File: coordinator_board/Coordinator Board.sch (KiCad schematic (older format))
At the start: 19 parts, among them P1 POWER, P4 SERIAL, SW1 Switch_SPDT_x2, SW2 Switch_DPST, U1 LM3671, U3 ESP-12E, U4 DIY-OLED-0.96, U5 SF303GJ26

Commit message: Finished updated schematic
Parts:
- removed P1: POWER, PH_Connector:S2B-PH-K-S, symbol CONN_01X02
- removed R8: 0, Resistors_SMD:R_0805_HandSoldering, symbol R
- added J1, J2, J3, J4: Conn_01x04, Pin_Headers:Pin_Header_Angled_1x04_Pitch2.54mm, symbol Conn_01x04
- added U6, U7: CD40109B, Housings_SSOP:TSSOP-24_4.4x7.8mm_Pitch0.65mm, symbol CD40109B
- added U8: 10118194, symbol 10118194
- R7: value 0 -> R
- RP1: footprint R_Array:R_Array_Concave_4x0805 -> nebrius-discrete:R_Array_Concave_4x0805
- SW2: footprint KMR6:KMR641NG -> nebrius-switch:KMR641NG
- U4: footprint DIY-OLED:DIY-OLED-0.96 -> nebrius-lcd:DIY-OLED-0.96
- U5: footprint SF303GJ26:SF303GJ26 -> nebrius-switch:SF303GJ26
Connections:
- net labels added: +5V
- wire segments 84 -> 177
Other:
- moved on the sheet: C1, C2, L1, P4, R1, R2, R4, R5, R6, RP1, SW1A, SW2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

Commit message: Fixed ESP footprint
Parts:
- U3: footprint ESP8266:ESP-12 -> ESP8266:ESP-12E_SMD
- U8: footprint (none) -> nebrius-conn:10118194
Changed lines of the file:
@@
 F 0 "U3" H 7400 4450 50  0000 C CNN
 F 1 "ESP-12E" H 7400 4650 50  0000 C CNN
-F 2 "ESP8266:ESP-12" H 7400 4550 50  0001 C CNN
+F 2 "ESP8266:ESP-12E_SMD" H 7400 4550 50  0001 C CNN
 F 3 "" H 7400 4550 50  0001 C CNN
 	1    7400 4550
@@
 F 0 "U8" V 1350 4950 60  0000 C CNN
 F 1 "10118194" H 1750 5050 60  0000 C CNN
-F 2 "" H 1850 4750 60  0001 C CNN
+F 2 "nebrius-conn:10118194" H 1850 4750 60  0001 C CNN
 F 3 "" H 1850 4750 60  0001 C CNN
 	1    1850 4750

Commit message: Finalized first draft of new schematic
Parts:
- removed U8: 10118194, nebrius-conn:10118194, symbol 10118194
- added D1: LED, LEDs:LED_1206_HandSoldering, symbol LED
- added R8: 0, Resistors_SMD:R_0805_HandSoldering, symbol R
- added U0: 10118194, nebrius-conn:10118194, symbol 10118194
- R7: value R -> 10k
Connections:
- net +5V: now also C1.1, SW1.2 (B), U1.1 (VIN), U1.3 (EN); no longer SW1.1 (A)
- net GND: now also R8.2, U0.5 (GND)
- net at U3.20 (GPIO10): now also D1.2 (A)
- new net: SW1.1 (A), U0.1 (Vcc)
- new net: D1.1 (K), R8.1
- no-connect marks 9 -> 8
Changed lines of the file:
@@
 EESchema Schematic File Version 2
+LIBS:Coordinator Board-rescue
 LIBS:power
 LIBS:device
@@
 	3600 4600 3650 4600
 Wire Wire Line
-	3750 4050 3750 4250
-Wire Wire Line
-	3750 4250 2600 4250
+	3750 4250 3750 3700
+Wire Wire Line
+	2600 4250 3750 4250
 Wire Wire Line
 	2600 4250 2600 4350
@@
 	8550 6400 10150 6400
 Wire Wire Line
-	10150 6400 10150 3500
+	10150 6400 10150 3550
 $Comp
 L Conn_01x04 J1
@@
 	1    0    0    -1
 $EndComp
-Connection ~ 2450 3950
-Wire Wire Line
-	2450 3700 2450 5050
 $Comp
 L +5V #PWR017
 U 1 1 5A47E663
-P 2450 3700
-F 0 "#PWR017" H 2450 3550 50  0001 C CNN
-F 1 "+5V" H 2450 3840 50  0000 C CNN
-F 2 "" H 2450 3700 50  0001 C CNN
-F 3 "" H 2450 3700 50  0001 C CNN
-	1    2450 3700
+P 3750 3700
+F 0 "#PWR017" H 3750 3550 50  0001 C CNN
+F 1 "+5V" H 3750 3840 50  0000 C CNN
+F 2 "" H 3750 3700 50  0001 C CNN
+F 3 "" H 3750 3700 50  0001 C CNN
+	1    3750 3700
 	1    0    0    -1
 $EndComp
@@
 	9950 4250 9950 6000
 Wire Wire Line
-	10150 3500 7450 3500
+	10150 3550 7450 3550
 $Comp
 L R R7
@@
 P 9700 5200
 F 0 "R7" V 9780 5200 50  0000 C CNN
-F 1 "R" V 9700 5200 50  0000 C CNN
+F 1 "10k" V 9700 5200 50  0000 C CNN
 F 2 "Resistors_SMD:R_0805_HandSoldering" V 9630 5200 50  0001 C CNN
 F 3 "" H 9700 5200 50  0001 C CNN
@@
 Connection ~ 10150 5450
 Wire Wire Line
-	7450 3500 7450 3650
+	7450 3550 7450 3650
 NoConn ~ 7650 3650
 NoConn ~ 7550 3650
-NoConn ~ 7350 3650
 $Comp
 L CD40109B U7
@@
 Wire Wire Line
 	2450 5050 2050 5050
-NoConn ~ 2050 4750
-NoConn ~ 2050 4850
-NoConn ~ 2050 4950
-$Comp
-L 10118194 U8
-U 1 1 5A48327E
+Wire Wire Line
+	2450 3950 2450 5050
+Connection ~ 3750 4050
+$Comp
+L LED D1
+U 1 1 5A4B428E
+P 10650 3800
+F 0 "D1" H 10650 3900 50  0000 C CNN
+F 1 "LED" H 10650 3700 50  0000 C CNN
+F 2 "LEDs:LED_1206_HandSoldering" H 10650 3800 50  0001 C CNN
+F 3 "" H 10650 3800 50  0001 C CNN
+	1    10650 3800
+	0    -1   -1   0
+$EndComp
+$Comp
+L R R8
+U 1 1 5A4B4365
+P 10650 4250
+F 0 "R8" V 10730 4250 50  0000 C CNN
+F 1 "0" V 10650 4250 50  0000 C CNN
+F 2 "Resistors_SMD:R_0805_HandSoldering" V 10580 4250 50  0001 C CNN
+F 3 "" H 10650 4250 50  0001 C CNN
+	1    10650 4250
+	1    0    0    -1
+$EndComp
+$Comp
+L GND #PWR024
+U 1 1 5A4B43F0
+P 10650 4550
+F 0 "#PWR024" H 10650 4300 50  0001 C CNN
+F 1 "GND" H 10650 4400 50  0000 C CNN
+F 2 "" H 10650 4550 50  0001 C CNN
+F 3 "" H 10650 4550 50  0001 C CNN
+	1    10650 4550
+	1    0    0    -1
+$EndComp
+Wire Wire Line
+	10650 4550 10650 4400
+Wire Wire Line
+	10650 4100 10650 3950
+Wire Wire Line
+	7350 3650 7350 3450
+Wire Wire Line
+	7350 3450 10650 3450
+Wire Wire Line
+	10650 3450 10650 3650
+$Comp
+L 10118194 U0
+U 1 1 5A5AABAF
 P 1850 4750
-F 0 "U8" V 1350 4950 60  0000 C CNN
+F 0 "U0" H 1750 5250 60  0000 C CNN
 F 1 "10118194" H 1750 5050 60  0000 C CNN
 F 2 "nebrius-conn:10118194" H 1850 4750 60  0001 C CNN
@@
 	0    -1   -1   0
 $EndComp
+NoConn ~ 2050 4750
+NoConn ~ 2050 4850
+NoConn ~ 2050 4950
 $EndSCHEMATC

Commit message: Finished most of the layout
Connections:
- net at SW1.1 (A): no longer U0.1 (Vcc)
- net at SW1.3 (C): now also U0.1 (Vcc)
- net at U3.13 (GPIO4): now also RP1.4 (P4), U5.4 (B); no longer U4.4 (SDA)
- net at U3.14 (GPIO5): now also RP1.3 (P3), U5.6 (D); no longer U4.3 (SCL)
- net at R7.2, U3.19 (GPIO9): now also U5.1 (A); no longer U5.2 (BTN)
- new net: U3.4 (GPIO16), U4.3 (SCL)
- new net: U3.5 (GPIO14), U4.4 (SDA)
- new net: RP1.2 (P2), U3.6 (GPIO12), U5.2 (BTN)
- new net: RP1.1 (P1), U3.7 (GPIO13), U5.3 (C)
- no-connect marks 8 -> 9
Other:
- moved on the sheet: R5, R6, R7, RP1, U4, U5

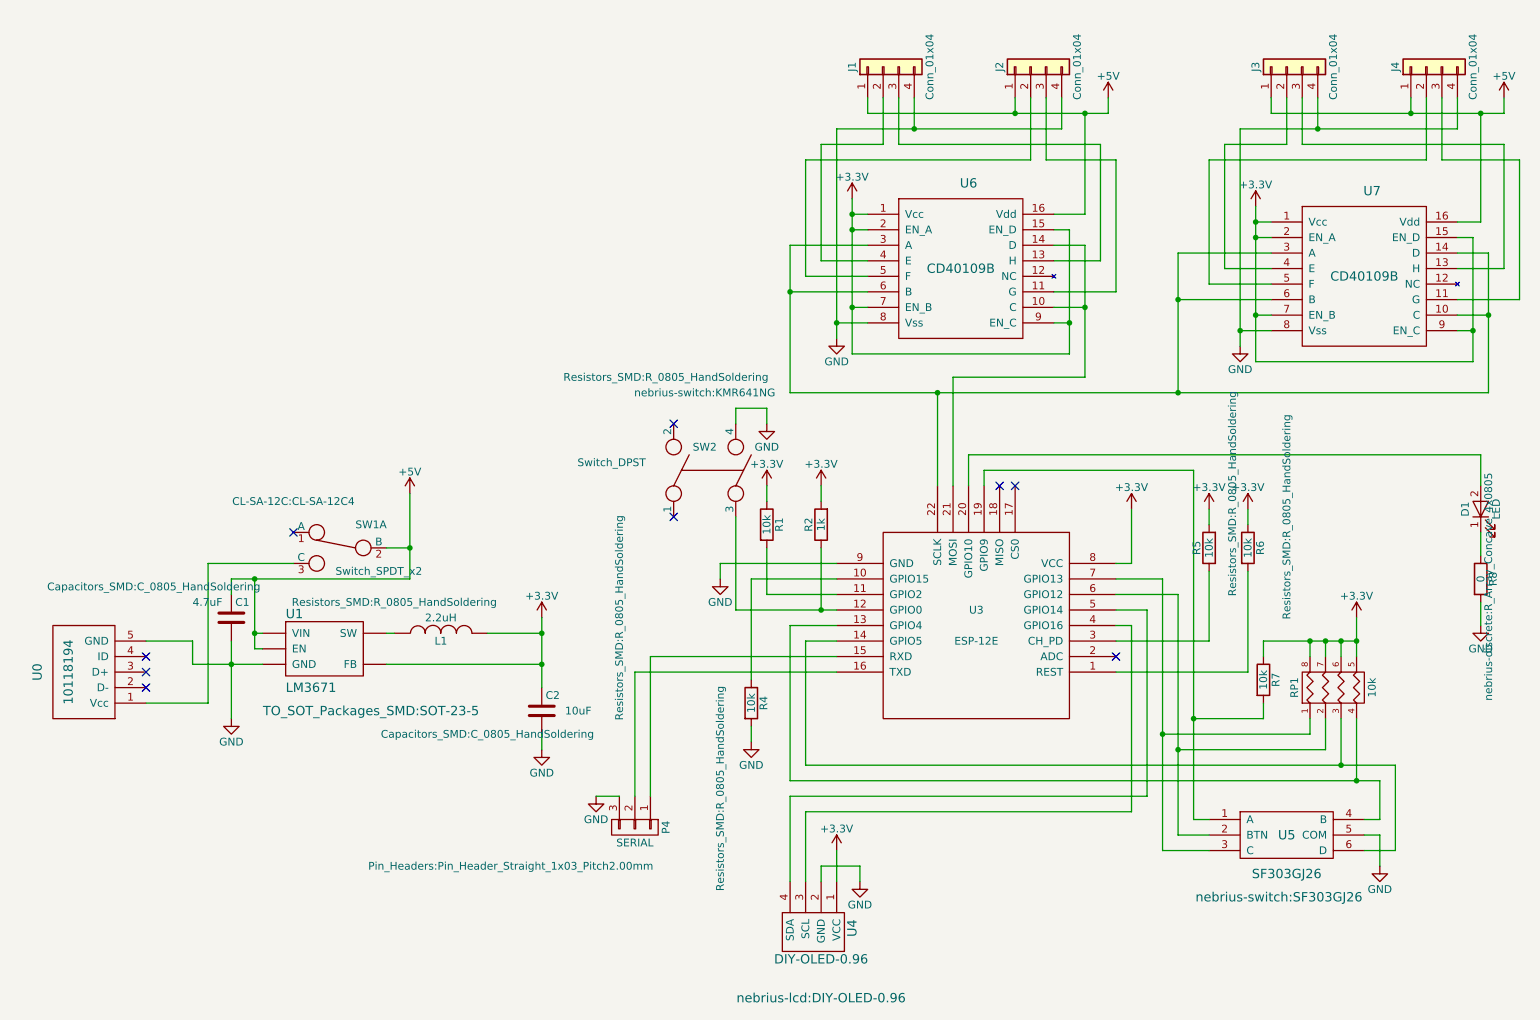
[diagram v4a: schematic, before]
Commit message: Revised schematic and added BOM
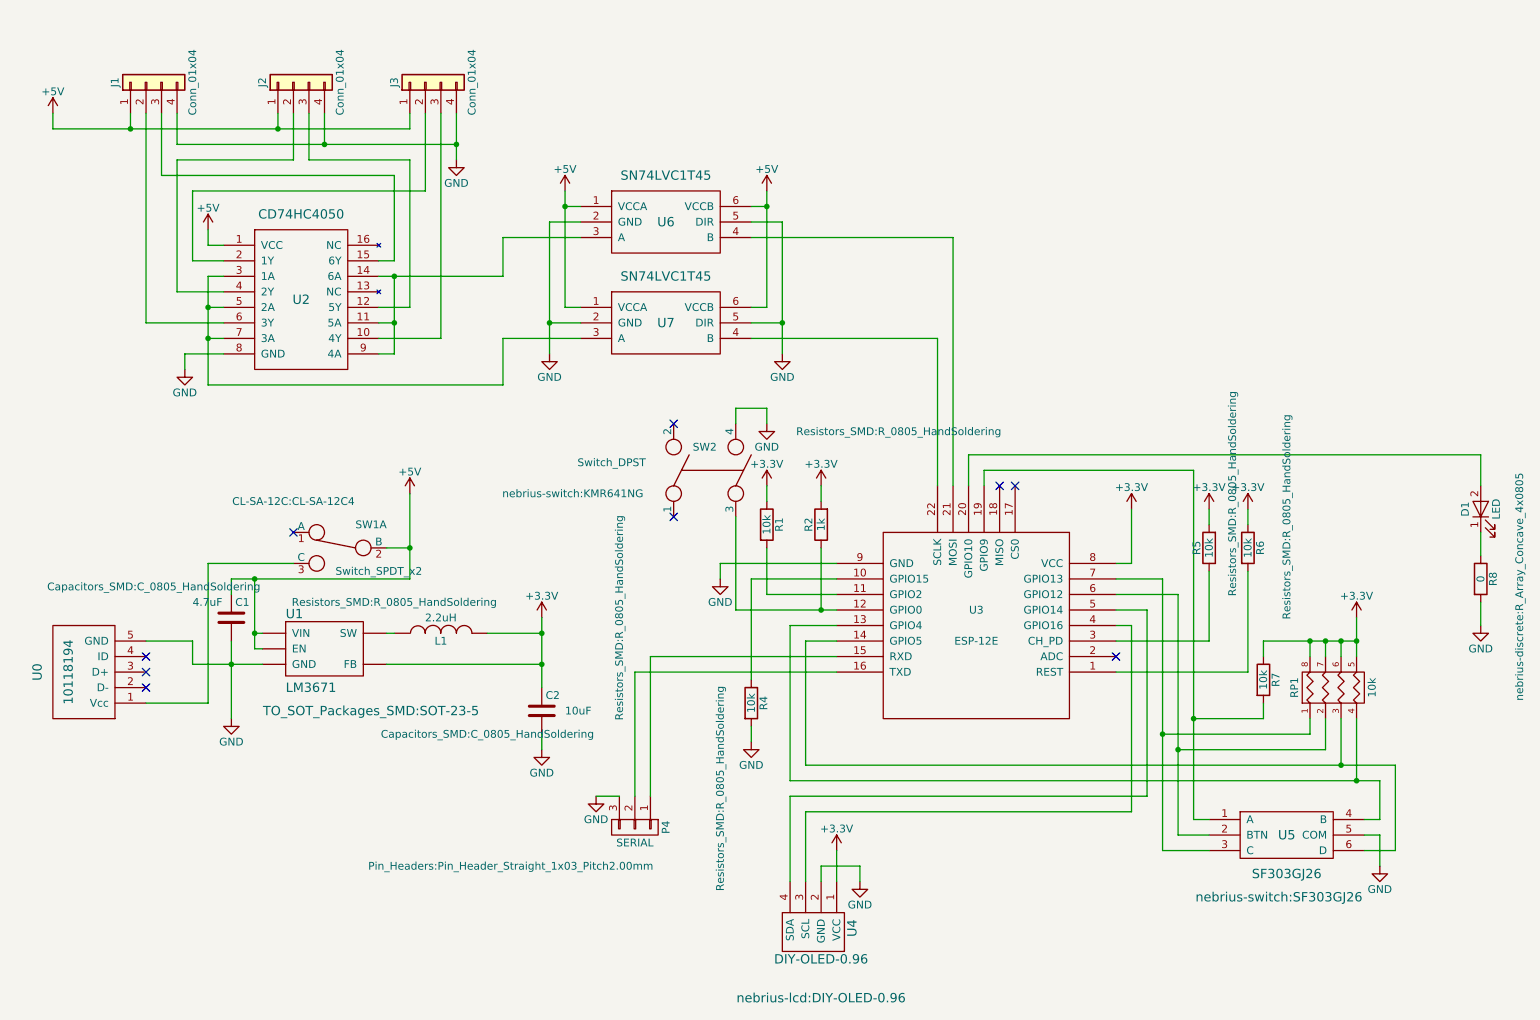
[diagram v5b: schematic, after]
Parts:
- removed J4: Conn_01x04, Pin_Headers:Pin_Header_Angled_1x04_Pitch2.54mm, symbol Conn_01x04
- removed U6, U7: CD40109B, Housings_SSOP:TSSOP-24_4.4x7.8mm_Pitch0.65mm, symbol CD40109B
- added U2: CD74HC4050, Housings_SOIC:SOIC-16W_5.3x10.2mm_Pitch1.27mm, symbol CD74HC4050
- added U6, U7: SN74LVC1T45, TO_SOT_Packages_SMD:SOT-23-6_Handsoldering, symbol SN74LVC1T45
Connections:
- net +5V: now also U2.1 (VCC), U6.1 (VCCA), U6.6 (VCCB), U7.1 (VCCA), U7.6 (VCCB)
- net GND: now also U2.8 (GND), U6.2 (GND), U6.5 (DIR), U7.2 (GND), U7.5 (DIR)
- net at U3.21 (MOSI): now also U6.4 (B)
- net at U3.22 (SCLK): now also U7.4 (B)
- net at J1.2 (Pin_2): now also U2.6 (3Y)
- net at J1.3 (Pin_3): now also U2.15 (6Y)
- net at J2.2 (Pin_2): now also U2.4 (2Y)
- net at J2.3 (Pin_3): now also U2.12 (5Y)
- net at J3.3 (Pin_3): now also U2.10 (4Y)
- net at J3.2 (Pin_2): now also U2.2 (1Y)
- new net: U2.11 (5A), U2.14 (6A), U2.9 (4A), U6.3 (A)
- new net: U2.3 (1A), U2.5 (2A), U2.7 (3A), U7.3 (A)
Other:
- moved on the sheet: J1, J2, J3

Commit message: Added some better surge protection
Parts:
- added C3: 0.1uF, symbol C
- added C4, C5, C6: 10uF, Resistors_SMD:R_0805_HandSoldering, symbol C
- added F0: Fuse, Resistors_SMD:R_0805_HandSoldering, symbol Fuse
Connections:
- net +3V3: now also C3.1
- net +5V: now also C4.2, C5.2, C6.2
- net GND: now also C3.2, C4.1, C5.1, C6.1
- net at SW1.3 (C): now also F0.1; no longer U0.1 (Vcc)
- new net: F0.2, U0.1 (Vcc)
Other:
- moved on the sheet: U0

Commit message: Added power planes and small tweaks
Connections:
- net +3V3: now also U6.6 (VCCB), U7.6 (VCCB)
- net +5V: no longer U6.6 (VCCB), U7.6 (VCCB)
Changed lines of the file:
@@
 	9150 4850 9150 4200
 $Comp
-L +3.3V #PWR8
+L +3.3V #PWR01
 U 1 1 58D6E218
 P 4600 4500
-F 0 "#PWR8" H 4600 4350 50  0001 C CNN
+F 0 "#PWR01" H 4600 4350 50  0001 C CNN
 F 1 "+3.3V" H 4600 4640 50  0000 C CNN
 F 2 "" H 4600 4500 50  0000 C CNN
@@
 $EndComp
 $Comp
-L +3.3V #PWR17
+L +3.3V #PWR02
 U 1 1 58D6E2FE
 P 6050 3650
-F 0 "#PWR17" H 6050 3500 50  0001 C CNN
+F 0 "#PWR02" H 6050 3500 50  0001 C CNN
 F 1 "+3.3V" H 6050 3790 50  0000 C CNN
 F 2 "" H 6050 3650 50  0000 C CNN
@@
 $EndComp
 $Comp
-L +3.3V #PWR20
+L +3.3V #PWR03
 U 1 1 58D6E3A2
 P 6500 6000
-F 0 "#PWR20" H 6500 5850 50  0001 C CNN
+F 0 "#PWR03" H 6500 5850 50  0001 C CNN
 F 1 "+3.3V" H 6500 6140 50  0000 C CNN
 F 2 "" H 6500 6000 50  0000 C CNN
@@
 	6500 6000 6500 6200
 $Comp
-L +3.3V #PWR19
+L +3.3V #PWR04
 U 1 1 58D6E5CC
 P 6400 3650
-F 0 "#PWR19" H 6400 3500 50  0001 C CNN
+F 0 "#PWR04" H 6400 3500 50  0001 C CNN
 F 1 "+3.3V" H 6400 3790 50  0000 C CNN
 F 2 "" H 6400 3650 50  0000 C CNN
@@
 $EndComp
 $Comp
-L +3.3V #PWR23
+L +3.3V #PWR05
 U 1 1 58D6E79B
 P 8900 3800
-F 0 "#PWR23" H 8900 3650 50  0001 C CNN
+F 0 "#PWR05" H 8900 3650 50  0001 C CNN
 F 1 "+3.3V" H 8900 3940 50  0000 C CNN
 F 2 "" H 8900 3800 50  0000 C CNN
@@
 $EndComp
 $Comp
-L +3.3V #PWR24
+L +3.3V #PWR06
 U 1 1 58D6E7CF
 P 9150 3800
-F 0 "#PWR24" H 9150 3650 50  0001 C CNN
+F 0 "#PWR06" H 9150 3650 50  0001 C CNN
 F 1 "+3.3V" H 9150 3940 50  0000 C CNN
 F 2 "" H 9150 3800 50  0000 C CNN
@@
 $EndComp
 $Comp
-L +3.3V #PWR22
+L +3.3V #PWR07
 U 1 1 58D6E803
 P 8400 3800
-F 0 "#PWR22" H 8400 3650 50  0001 C CNN
+F 0 "#PWR07" H 8400 3650 50  0001 C CNN
 F 1 "+3.3V" H 8400 3940 50  0000 C CNN
 F 2 "" H 8400 3800 50  0000 C CNN
@@
 	6500 4250 5950 4250
 $Comp
-L GND #PWR14
+L GND #PWR08
 U 1 1 58D6ED20
 P 5950 5300
-F 0 "#PWR14" H 5950 5050 50  0001 C CNN
+F 0 "#PWR08" H 5950 5050 50  0001 C CNN
 F 1 "GND" H 5950 5150 50  0000 C CNN
 F 2 "" H 5950 5300 50  0000 C CNN
@@
 	5950 5200 5950 5300
 $Comp
-L GND #PWR4
+L GND #PWR09
 U 1 1 58D6F166
 P 2600 5150
-F 0 "#PWR4" H 2600 4900 50  0001 C CNN
+F 0 "#PWR09" H 2600 4900 50  0001 C CNN
 F 1 "GND" H 2600 5000 50  0000 C CNN
 F 2 "" H 2600 5150 50  0000 C CNN
@@
 $EndComp
 $Comp
-L GND #PWR9
+L GND #PWR010
 U 1 1 58D6F261
 P 4600 5350
-F 0 "#PWR9" H 4600 5100 50  0001 C CNN
+F 0 "#PWR010" H 4600 5100 50  0001 C CNN
 F 1 "GND" H 4600 5200 50  0000 C CNN
 F 2 "" H 4600 5350 50  0000 C CNN
@@
 	4600 5250 4600 5350
 $Comp
-L GND #PWR13
+L GND #PWR011
 U 1 1 58D6F42E
 P 5750 4250
-F 0 "#PWR13" H 5750 4000 50  0001 C CNN
+F 0 "#PWR011" H 5750 4000 50  0001 C CNN
 F 1 "GND" H 5750 4100 50  0000 C CNN
 F 2 "" H 5750 4250 50  0000 C CNN
@@
 $EndComp
 $Comp
-L GND #PWR12
+L GND #PWR012
 U 1 1 58D6F4C6
 P 4950 5650
-F 0 "#PWR12" H 4950 5400 50  0001 C CNN
+F 0 "#PWR012" H 4950 5400 50  0001 C CNN
 F 1 "GND" H 4950 5500 50  0000 C CNN
 F 2 "" H 4950 5650 50  0000 C CNN
@@
 	5100 5650 4950 5650
 $Comp
-L GND #PWR21
+L GND #PWR013
 U 1 1 58D6F646
 P 6650 6200
-F 0 "#PWR21" H 6650 5950 50  0001 C CNN
+F 0 "#PWR013" H 6650 5950 50  0001 C CNN
 F 1 "GND" H 6650 6050 50  0000 C CNN
 F 2 "" H 6650 6200 50  0000 C CNN
@@
 $EndComp
 $Comp
-L GND #PWR26
+L GND #PWR014
 U 1 1 5953540A
 P 10000 6100
-F 0 "#PWR26" H 10000 5850 50  0001 C CNN
+F 0 "#PWR014" H 10000 5850 50  0001 C CNN
 F 1 "GND" H 10000 5950 50  0000 C CNN
 F 2 "" H 10000 6100 50  0000 C CNN
@@
 $EndComp
 $Comp
-L GND #PWR16
+L GND #PWR015
 U 1 1 59615099
 P 6050 3250
-F 0 "#PWR16" H 6050 3000 50  0001 C CNN
+F 0 "#PWR015" H 6050 3000 50  0001 C CNN
 F 1 "GND" H 6050 3100 50  0000 C CNN
 F 2 "" H 6050 3250 50  0000 C CNN
@@
 $EndComp
 $Comp
-L +3.3V #PWR25
+L +3.3V #PWR016
 U 1 1 59616333
 P 9850 4500
-F 0 "#PWR25" H 9850 4350 50  0001 C CNN
+F 0 "#PWR016" H 9850 4350 50  0001 C CNN
 F 1 "+3.3V" H 9850 4640 50  0000 C CNN
 F 2 "" H 9850 4500 50  0000 C CNN
@@
 $EndComp
 $Comp
-L +5V #PWR5
+L +5V #PWR017
 U 1 1 5A47E663
 P 3750 3700
-F 0 "#PWR5" H 3750 3550 50  0001 C CNN
+F 0 "#PWR017" H 3750 3550 50  0001 C CNN
 F 1 "+5V" H 3750 3840 50  0000 C CNN
 F 2 "" H 3750 3700 50  0001 C CNN
@@
 $EndComp
 $Comp
-L +5V #PWR1
+L +5V #PWR018
 U 1 1 5A47E6D7
 P 1450 1250
-F 0 "#PWR1" H 1450 1100 50  0001 C CNN
+F 0 "#PWR018" H 1450 1100 50  0001 C CNN
 F 1 "+5V" H 1450 1390 50  0000 C CNN
 F 2 "" H 1450 1250 50  0001 C CNN
@@
 $EndComp
 $Comp
-L GND #PWR2
+L GND #PWR019
 U 1 1 5A47ECA2
 P 2300 2900
-F 0 "#PWR2" H 2300 2650 50  0001 C CNN
+F 0 "#PWR019" H 2300 2650 50  0001 C CNN
 F 1 "GND" H 2300 2750 50  0000 C CNN
 F 2 "" H 2300 2900 50  0001 C CNN
@@
 $EndComp
 $Comp
-L GND #PWR27
+L GND #PWR020
 U 1 1 5A4B43F0
 P 10650 4550
-F 0 "#PWR27" H 10650 4300 50  0001 C CNN
+F 0 "#PWR020" H 10650 4300 50  0001 C CNN
 F 1 "GND" H 10650 4400 50  0000 C CNN
 F 2 "" H 10650 4550 50  0001 C CNN
@@
 Wire Wire Line
 	7350 3650 7350 3450
-Wire Wire Line
-	7350 3450 10650 3450
 Wire Wire Line
 	10650 3450 10650 3650
@@
 Connection ~ 2900 1350
 $Comp
-L GND #PWR6
+L GND #PWR021
 U 1 1 5A6AE250
 P 4050 1550
-F 0 "#PWR6" H 4050 1300 50  0001 C CNN
+F 0 "#PWR021" H 4050 1300 50  0001 C CNN
 F 1 "GND" H 4050 1400 50  0000 C CNN
 F 2 "" H 4050 1550 50  0001 C CNN
@@
 	3850 1750 3850 1250
 $Comp
-L +5V #PWR3
+L +5V #PWR022
 U 1 1 5A6B5F5B
 P 2450 2000
-F 0 "#PWR3" H 2450 1850 50  0001 C CNN
+F 0 "#PWR022" H 2450 1850 50  0001 C CNN
 F 1 "+5V" H 2450 2140 50  0000 C CNN
 F 2 "" H 2450 2000 50  0001 C CNN
@@
 Connection ~ 6050 1850
 $Comp
-L GND #PWR10
+L GND #PWR023
 U 1 1 5A6B6F9C
 P 4650 2800
-F 0 "#PWR10" H 4650 2550 50  0001 C CNN
+F 0 "#PWR023" H 4650 2550 50  0001 C CNN
 F 1 "GND" H 4650 2650 50  0000 C CNN
 F 2 "" H 4650 2800 50  0001 C CNN
@@
 $EndComp
 $Comp
-L GND #PWR18
+L GND #PWR024
 U 1 1 5A6B7018
 P 6150 2800
-F 0 "#PWR18" H 6150 2550 50  0001 C CNN
+F 0 "#PWR024" H 6150 2550 50  0001 C CNN
 F 1 "GND" H 6150 2650 50  0000 C CNN
 F 2 "" H 6150 2800 50  0001 C CNN
@@
 Connection ~ 4650 2600
 $Comp
-L +5V #PWR11
+L +5V #PWR025
 U 1 1 5A6B779E
 P 4750 1750
-F 0 "#PWR11" H 4750 1600 50  0001 C CNN
+F 0 "#PWR025" H 4750 1600 50  0001 C CNN
 F 1 "+5V" H 4750 1890 50  0000 C CNN
 F 2 "" H 4750 1750 50  0001 C CNN
 F 3 "" H 4750 1750 50  0001 C CNN
 	1    4750 1750
-	1    0    0    -1
-$EndComp
-$Comp
-L +5V #PWR15
-U 1 1 5A6B7834
-P 6050 1750
-F 0 "#PWR15" H 6050 1600 50  0001 C CNN
-F 1 "+5V" H 6050 1890 50  0000 C CNN
-F 2 "" H 6050 1750 50  0001 C CNN
-F 3 "" H 6050 1750 50  0001 C CNN
-	1    6050 1750
 	1    0    0    -1
 $EndComp
@@
 $EndComp
 $Comp
-L GND #PWR7
+L GND #PWR027
 U 1 1 5A6BBB68
 P 4300 5350
-F 0 "#PWR7" H 4300 5100 50  0001 C CNN
+F 0 "#PWR027" H 4300 5100 50  0001 C CNN
 F 1 "GND" H 4300 5200 50  0000 C CNN
 F 2 "" H 4300 5350 50  0001 C CNN
@@
 Wire Wire Line
 	2450 5050 2350 5050
+$Comp
+L +3.3V #PWR?
+U 1 1 5A6BE1B6
+P 6050 1750
+F 0 "#PWR?" H 6050 1600 50  0001 C CNN
+F 1 "+3.3V" H 6050 1890 50  0000 C CNN
+F 2 "" H 6050 1750 50  0001 C CNN
+F 3 "" H 6050 1750 50  0001 C CNN
+	1    6050 1750
+	1    0    0    -1
+$EndComp
+Wire Wire Line
+	7350 3450 10650 3450
 $EndSCHEMATC
